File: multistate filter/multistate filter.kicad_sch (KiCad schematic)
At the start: 14 parts, among them J1 VCC, J2 GND, J3 IN, J4 HP, J5 BP, J6 LP, U1 4069

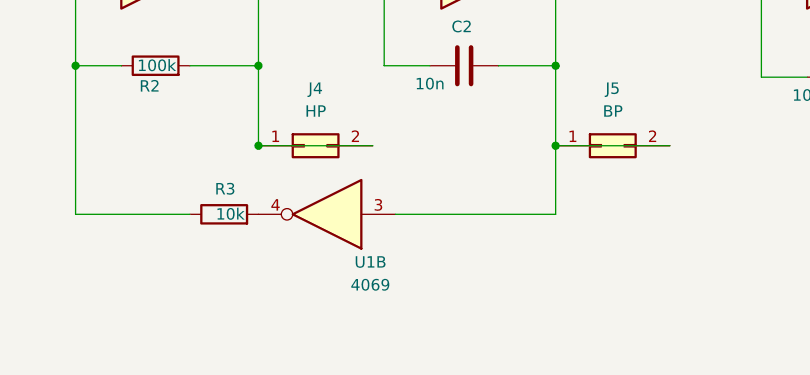
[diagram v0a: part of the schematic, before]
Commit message: multistate filter with potentiometer
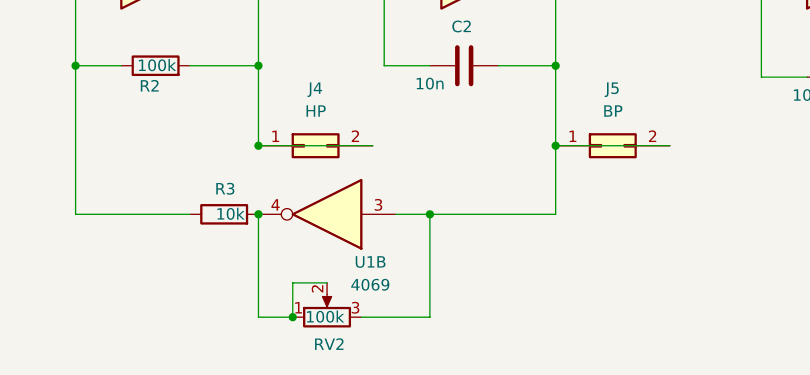
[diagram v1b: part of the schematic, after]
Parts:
- added RV2: 100k, Potentiometer_THT:Potentiometer_Alps_RK163_Single_Horizontal, symbol Device:R_Potentiometer
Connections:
- net at C2.2, J5.1 (Pin_1), J5.2 (Pin_2)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: now also RV2.3
- net at R3.2, U1.4: now also RV2.1, RV2.2
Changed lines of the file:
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@@
+	)
+	(junction
+		(at 95.25 147.32)
+		(diameter 0)
+		(color 0 0 0 0)
 	)
 	(junction
@@
 	)
 	(junction
+		(at 91.44 135.89)
+		(diameter 0)
+		(color 0 0 0 0)
+	)
+	(junction
 		(at 166.37 128.27)
 		(diameter 0)
@@
 	)
 	(junction
+		(at 110.49 135.89)
+		(diameter 0)
+		(color 0 0 0 0)
+	)
+	(junction
 		(at 224.79 20.32)
 		(diameter 0)
@@
 	(wire
 		(pts
+			(xy 102.87 147.32) (xy 110.49 147.32)
+		)
+		(stroke
+			(width 0)
+			(type default)
+		)
+	)
+	(wire
+		(pts
 			(xy 105.41 119.38) (xy 105.41 109.22)
 		)
@@
 	(wire
 		(pts
+			(xy 95.25 143.51) (xy 99.06 143.51)
+		)
+		(stroke
+			(width 0)
+			(type default)
+		)
+	)
+	(wire
+		(pts
 			(xy 91.44 128.27) (xy 104.14 128.27)
 		)
@@
 	(wire
 		(pts
+			(xy 110.49 147.32) (xy 110.49 135.89)
+		)
+		(stroke
+			(width 0)
+			(type default)
+		)
+	)
+	(wire
+		(pts
 			(xy 39.37 109.22) (xy 52.07 109.22)
 		)
@@
 	(wire
 		(pts
-			(xy 106.68 135.89) (xy 124.46 135.89)
+			(xy 106.68 135.89) (xy 110.49 135.89)
 		)
 		(stroke
@@
 	(wire
 		(pts
+			(xy 91.44 147.32) (xy 91.44 135.89)
+		)
+		(stroke
+			(width 0)
+			(type default)
+		)
+	)
+	(wire
+		(pts
 			(xy 91.44 109.22) (xy 95.25 109.22)
 		)
@@
 	(wire
 		(pts
+			(xy 110.49 135.89) (xy 124.46 135.89)
+		)
+		(stroke
+			(width 0)
+			(type default)
+		)
+	)
+	(wire
+		(pts
 			(xy 130.81 105.41) (xy 134.62 105.41)
 		)
@@
 	(wire
 		(pts
+			(xy 95.25 147.32) (xy 95.25 143.51)
+		)
+		(stroke
+			(width 0)
+			(type default)
+		)
+	)
+	(wire
+		(pts
 			(xy 91.44 119.38) (xy 91.44 109.22)
 		)
@@
 		(pts
 			(xy 147.32 109.22) (xy 147.32 120.65)
+		)
+		(stroke
+			(width 0)
+			(type default)
+		)
+	)
+	(wire
+		(pts
+			(xy 95.25 147.32) (xy 91.44 147.32)
 		)
 		(stroke
@@
 					(unit 1)
 				)
+			)
+		)
+	)
+	(symbol
+		(lib_id "Device:R_Potentiometer")
+		(at 99.06 147.32 90)
+		(unit 1)
+		(exclude_from_sim no)
+		(in_bom yes)
+		(on_board yes)
+		(dnp no)
+		(property "Reference" "RV2"
+			(at 99.314 150.368 90)
+			(effects
+				(font
+					(size 1.27 1.27)
+				)
+			)
+		)
+		(property "Value" "100k"
+			(at 98.806 147.32 90)
+			(effects
+				(font
+					(size 1.27 1.27)
+				)
+			)
+		)
+		(property "Footprint" "Potentiometer_THT:Potentiometer_Alps_RK163_Single_Horizontal"
+			(at 99.06 147.32 0)
+			(effects
+				(font
+					(size 1.27 1.27)
+				)
+				(hide yes)
+			)
+		)
+		(property "Datasheet" "~"
+			(at 99.06 147.32 0)
+			(effects
+				(font
+					(size 1.27 1.27)
+				)
+				(hide yes)
+			)
+		)
+		(property "Description" "Potentiometer"
+			(at 99.06 147.32 0)
+			(effects
+				(font
+					(size 1.27 1.27)
+				)
+				(hide yes)
+			)
+		)
+		(pin "3"
+		)
+		(pin "2"
+		)
+		(pin "1"
+		)
+		(instances
+			(project ""
+				(path "/1f3e0410-067a-4835-97d6-4663e9beff54"
+					(reference "RV2")
+					(unit 1)
+				)
